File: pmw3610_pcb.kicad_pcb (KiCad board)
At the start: 2 copper layers, 23.5 x 31.5 mm, 24 parts, among them J1 Conn_01x06, J2 Conn_01x08, U1 PMW3610, U2 TLV74318PDBVR

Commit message: feat: update PCB rev 1.1
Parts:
- removed the TP1 at (145.2, 114.2)
- C1: footprint Capacitor_SMD:C_0603_1608Metric -> Capacitor_SMD:C_0805_2012Metric
- C4: value 100nF X7R -> 100nF
- C6: value 10uF X7R -> 10uF; footprint Capacitor_SMD:C_0603_1608Metric -> Capacitor_SMD:C_0805_2012Metric
- C7: value 10nF X7R -> 10nF
- H1, H2, H3, H4: moved to B.Cu
- J1: value Conn_01x06 -> Conn_PinHeader; footprint Connector_PinHeader_2.54mm:PinHeader_1x06_P2.54mm_Vertical -> Connector_PinHeader_2.54mm:PinHeader_1x07_P2.54mm_Vertical
- J2: value Conn_01x08 -> Conn_FPC
- moved J1 0.90 mm to (139.9, 92.8)
- moved C6 0.28 mm to (159.5, 107.8)
- moved C1 0.21 mm to (159.5, 100.2)
- turned H1 to 180 degrees
- turned H2 to 180 degrees
- turned H3 to 180 degrees
- turned H4 to 180 degrees
- renumbered TP4 to TP1
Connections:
- net VIO renamed VDDIO
- J2 pad 8: unconnected-(J2-Pin_8-Pad8) -> nRESET
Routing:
- net GND: track 15.9 -> 73.9 mm, vias 19 -> 42
- net nRESET: track 9.82 -> 32.7 mm, vias 2 -> 0
- net MOTION: track 30.7 -> 32.8 mm
- net VIN: track 30.9 -> 28.8 mm
- net +1V8: track 29.2 -> 31.1 mm
- net nCS: track 30.9 -> 32.5 mm
- net VDDIO: track 43.3 -> 42.2 mm
- net SCLK: track 20.5 -> 19.8 mm
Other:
- board text added: "${COMPANY} ${TITLE} Rev ${REVISION}"
- board text added: "JP1: [1-2 3]V_{DDIO}=VIN [1 2-3]V_{DDIO}=1.8V"
- board text added: "~{CS}"
- board text added: "~{RST}"
- board text removed: "${TITLE} Rev ${REVISION}"
- board text removed: "JP1: [1-2 3]VIO=VIN [1 2-3]VIO=1.8V"
- board text removed: "nCS"

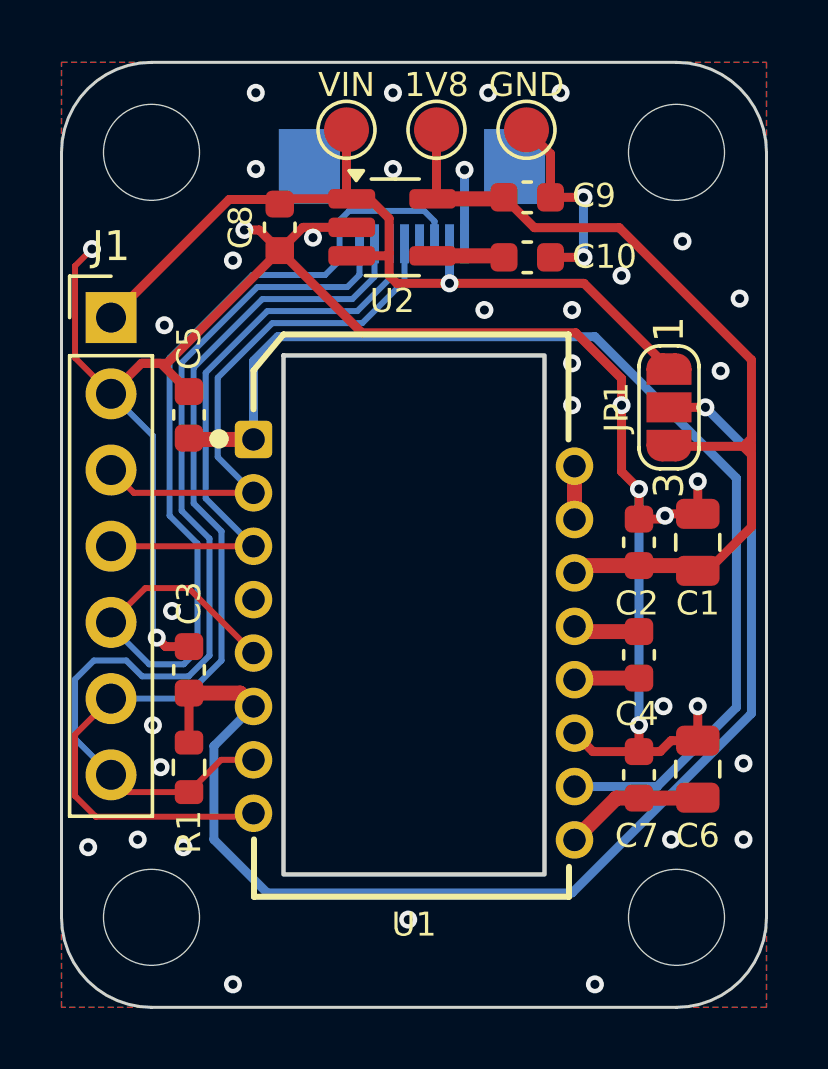
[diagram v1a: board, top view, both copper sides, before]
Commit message: feat: update PMW3610 footprint
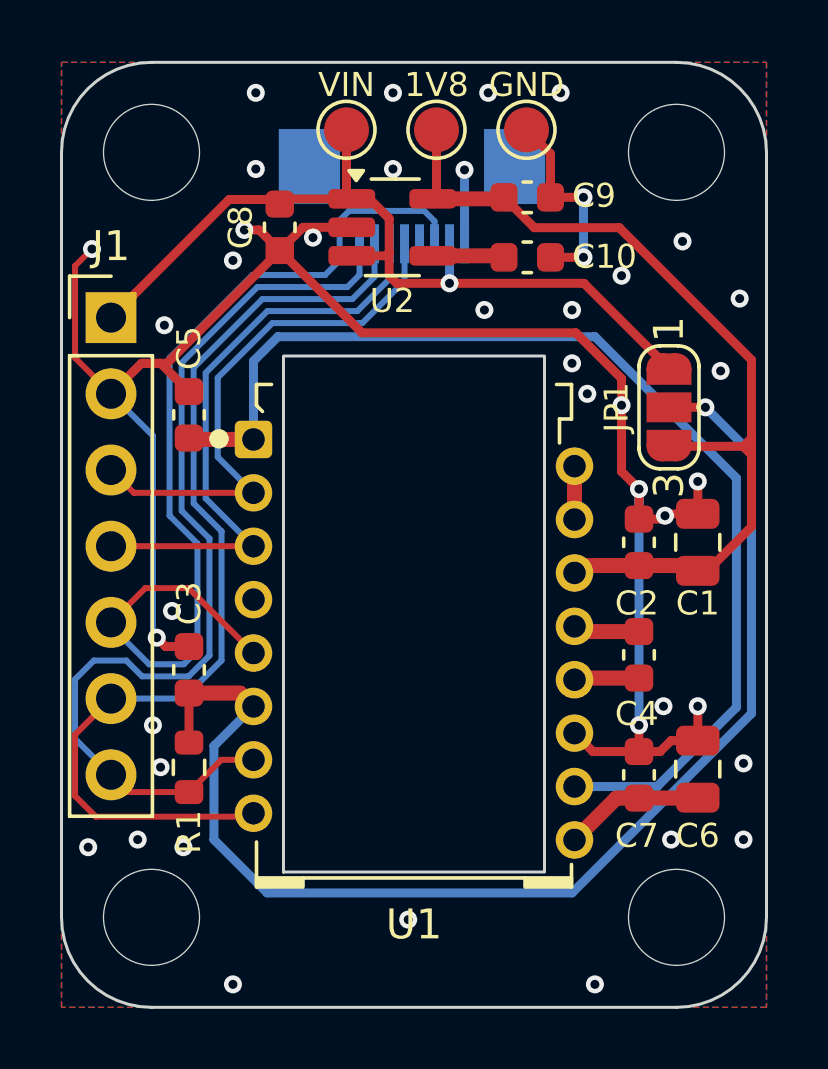
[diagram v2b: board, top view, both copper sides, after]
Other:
- board text added: "MOT"
- board text removed: "Mot"

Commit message: feat: increase the copper to board edge clearance to 0.4mm for better V-cut panelization
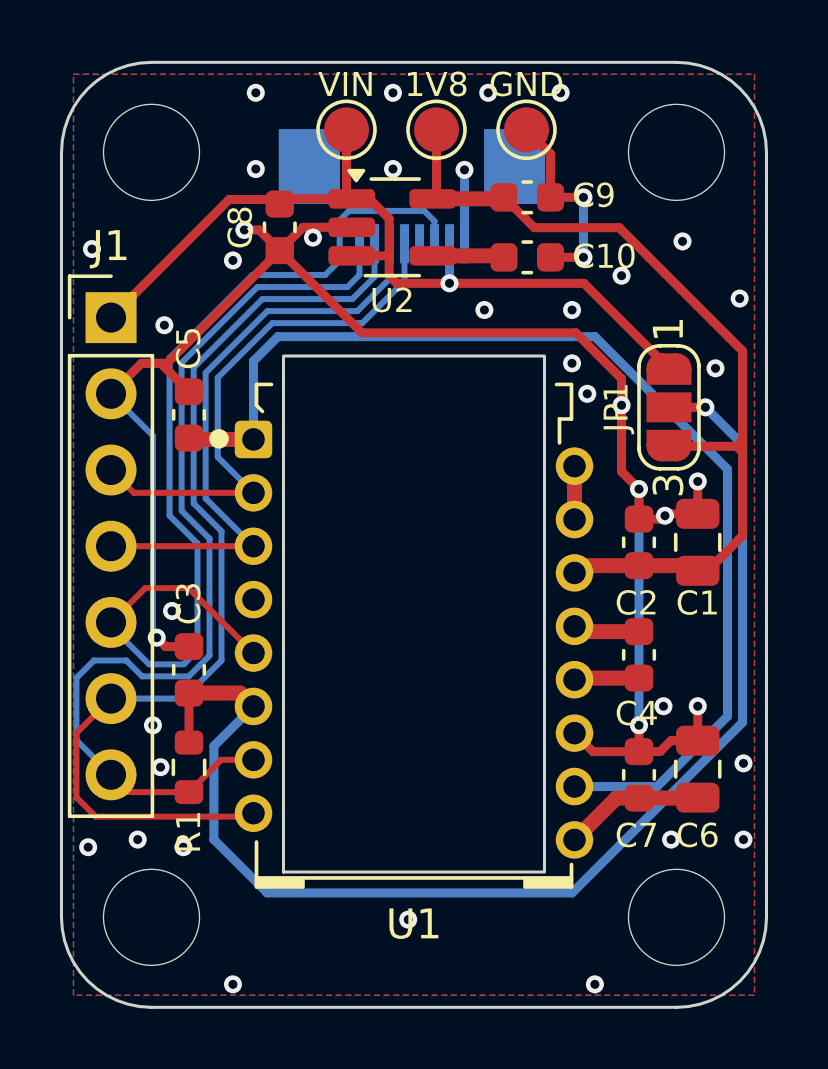
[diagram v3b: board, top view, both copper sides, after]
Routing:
- net GND: track 73.9 -> 68.3 mm
- net +1V8: track 31.1 -> 30.4 mm

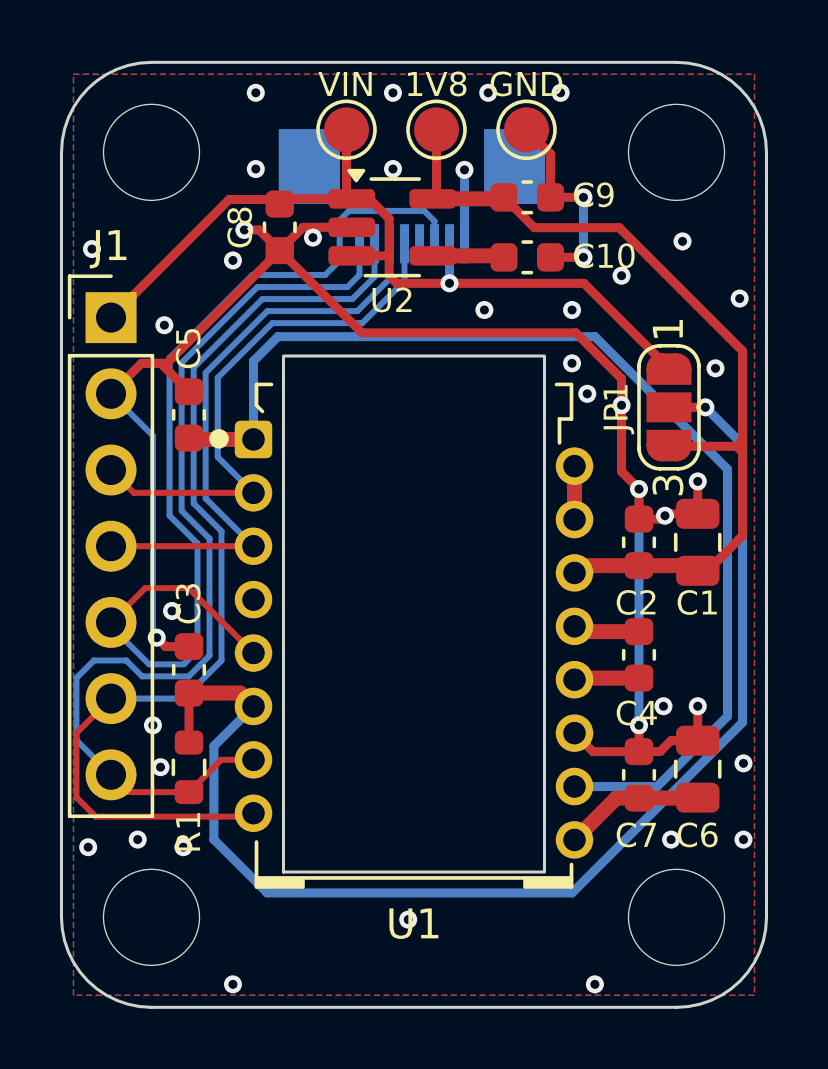
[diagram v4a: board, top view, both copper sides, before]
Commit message: feat: changed the J2 to the top layer
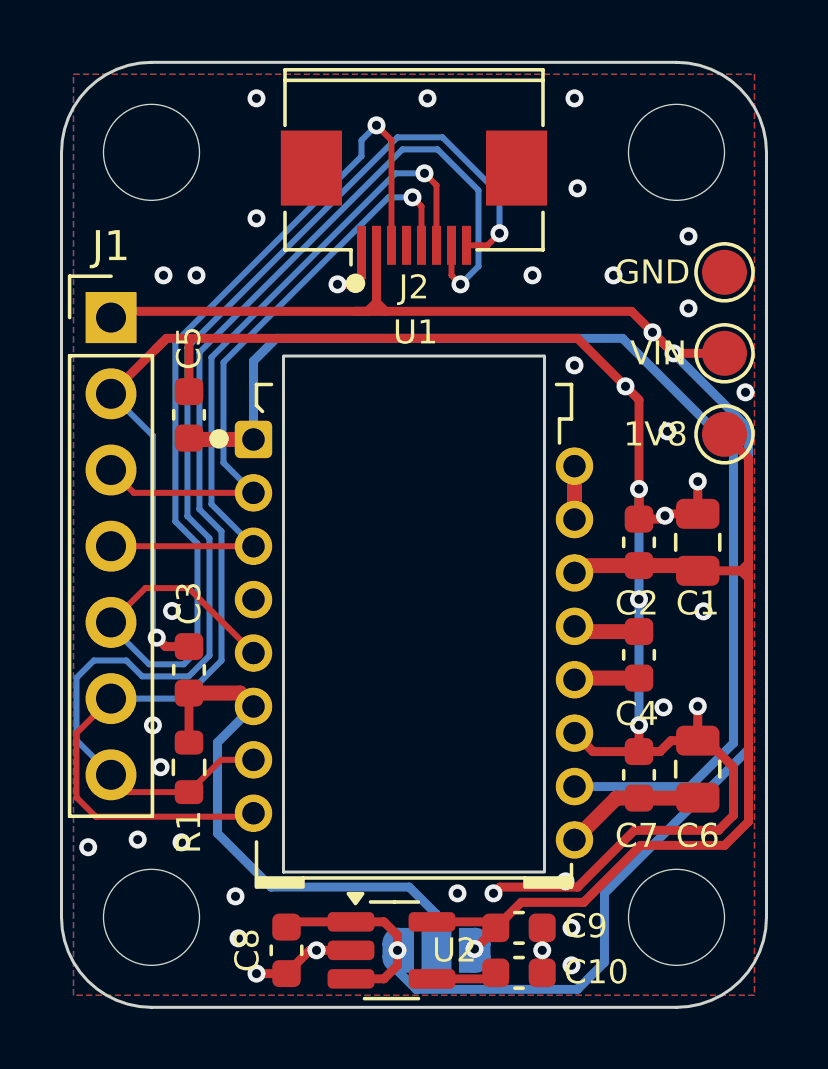
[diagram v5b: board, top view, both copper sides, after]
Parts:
- J2: moved to F.Cu
- JP1: moved to B.Cu
- moved C9 24.4 mm to (153.5, 113.1)
- moved C8 24.1 mm to (145.8, 113.8)
- moved U2 24.1 mm to (149.2, 113.8)
- moved C10 23.9 mm to (153.5, 114.6)
- moved JP1 19.7 mm to (150.8, 113.8), turned to 0 degrees
- moved TP2 14.6 mm to (160.3, 94.0)
- moved TP3 14.0 mm to (160.3, 96.7)
- moved TP1 8.13 mm to (160.3, 91.2)
- moved J2 0.08 mm to (150.0, 87.3), turned to 0 degrees
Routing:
- net VIN: track 28.8 -> 63.5 mm, vias 1 -> 3
- net VDDIO: track 41.9 -> 18.3 mm, vias 1 -> 0
- net MOTION: track 32.7 -> 42.3 mm, vias 0 -> 1
- net nRESET: track 32.6 -> 41.6 mm, vias 0 -> 1
- net SCLK: track 19.8 -> 23.8 mm, vias 0 -> 1
- net +1V8: track 30.4 -> 33.4 mm, vias 0 -> 1
- net nCS: track 32.5 -> 34.6 mm, vias 0 -> 1
- net GND: track 68.3 -> 70.3 mm, vias 42 -> 41
- net SDIO: track 18.2 -> 20.1 mm, vias 0 -> 1
- net Net-(U1-+VCSEL): track 37.1 -> 38.3 mm
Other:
- board text added: "JLCJLCJLCJLC"

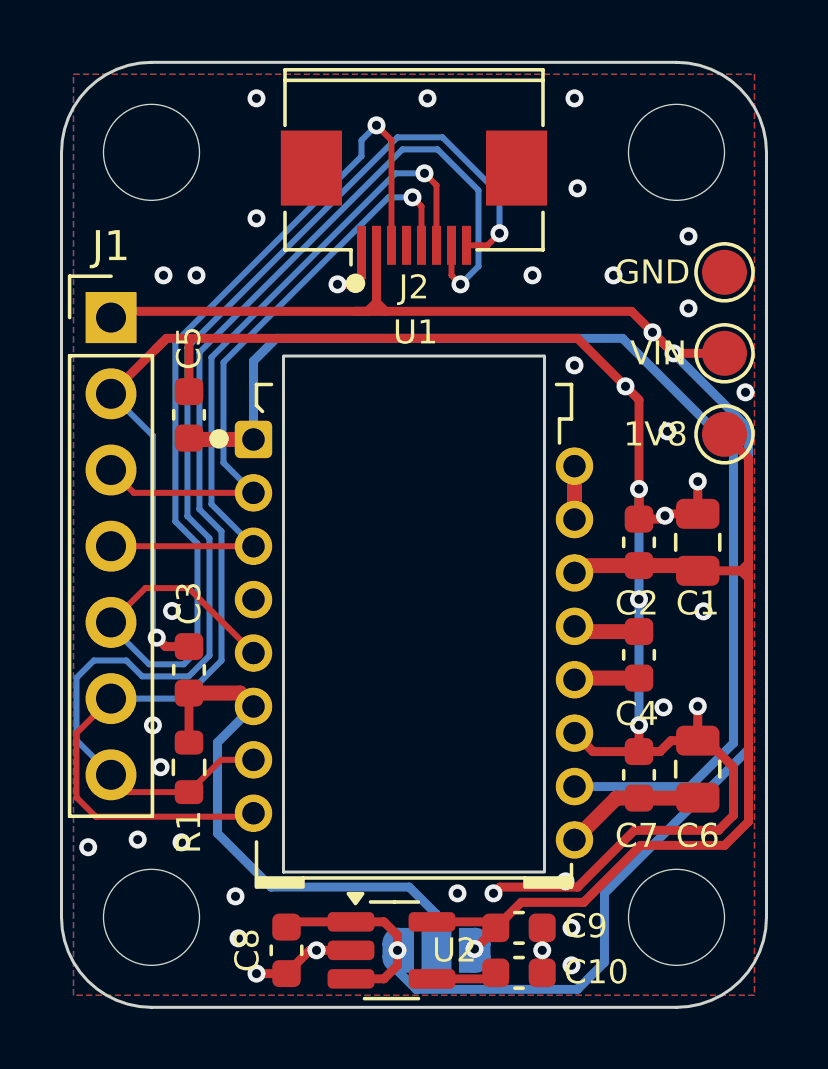
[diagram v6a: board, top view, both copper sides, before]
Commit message: feat: add axis mark
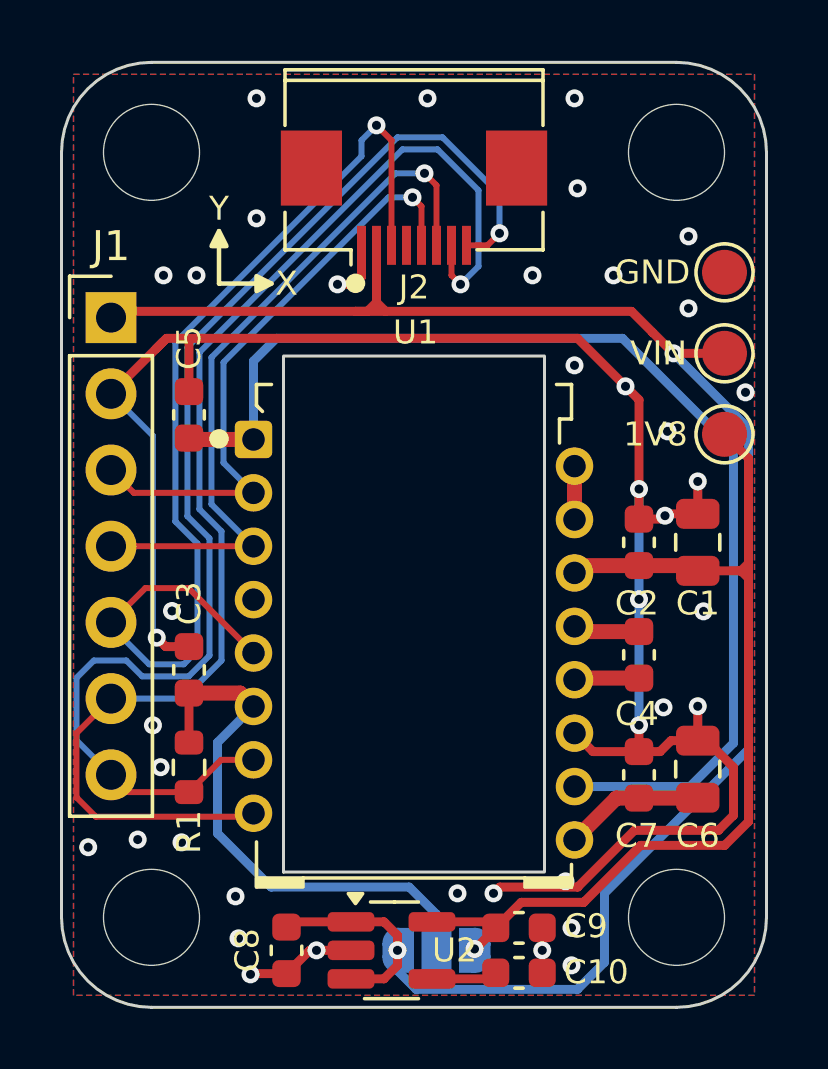
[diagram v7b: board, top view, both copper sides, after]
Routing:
- net VIN: track 63.5 -> 62.5 mm, vias 3 -> 2
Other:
- board text added: "X"
- board text added: "Y"
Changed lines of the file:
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@@
+		(layer "F.SilkS")
+	)
+	(gr_poly
+		(pts
+			(xy 144.75 91.375) (xy 145.25 91.625) (xy 144.75 91.875)
+		)
+		(stroke
+			(width 0.15)
+			(type solid)
+		)
+		(fill yes)
+		(layer "F.SilkS")
+	)
+	(gr_line
+		(start 143.5 89.875)
+		(end 143.5 91.625)
+		(stroke
+			(width 0.15)
+			(type default)
+		)
+		(layer "F.SilkS")
+	)
+	(gr_poly
+		(pts
+			(xy 143.25 90.375) (xy 143.5 89.875) (xy 143.75 90.375)
+		)
+		(stroke
+			(width 0.15)
+			(type solid)
+		)
+		(fill yes)
+		(layer "F.SilkS")
+	)
+	(gr_line
+		(start 143.5 91.625)
+		(end 145.25 91.625)
+		(stroke
+			(width 0.15)
+			(type default)
+		)
 		(layer "F.SilkS")
 	)
@@
 		(layer "Edge.Cuts")
 	)
+	(gr_text "Y"
+		(at 143.5 89.125 0)
+		(layer "F.SilkS")
+		(effects
+			(font
+				(size 0.8 0.8)
+				(thickness 0.125)
+			)
+		)
+	)
+	(gr_text "X"
+		(at 145.75 91.625 0)
+		(layer "F.SilkS")
+		(effects
+			(font
+				(size 0.8 0.8)
+				(thickness 0.125)
+			)
+		)
+	)
 	(gr_text "~{CS}"
 		(at 140.917 103.046 0)
@@
 	)
 	(segment
+		(start 144.55 114.65)
+		(end 144.575 114.625)
+		(width 0.3)
+		(layer "F.Cu")
+		(net 1)
+	)
+	(segment
 		(start 141.75 93.45)
 		(end 141.4 93.8)
@@
 	)
 	(segment
+		(start 144.575 114.625)
+		(end 145.75 114.625)
+		(width 0.3)
+		(layer "F.Cu")
+		(net 1)
+	)
+	(segment
 		(start 157.5 98.474)
 		(end 157.5 99.475)
@@
 	)
 	(segment
-		(start 144.75 114.625)
-		(end 145.75 114.625)
-		(width 0.3)
-		(layer "F.Cu")
-		(net 1)
-	)
-	(segment
 		(start 160.65 109.35)
 		(end 160.65 107.75)
@@
 	)
 	(via
-		(at 144.75 114.625)
+		(at 144.55 114.65)
 		(size 0.6)
 		(drill 0.3)
@@
 	)
 	(via
-		(at 157.95 93.25)
-		(size 0.6)
-		(drill 0.3)
-		(layers "F.Cu" "B.Cu")
-		(net 4)
-	)
-	(via
 		(at 158.65 93.95)
 		(size 0.6)
@@
 		(start 161.15 96.45)
 		(end 161.15 107.15)
-		(width 0.3)
-		(layer "B.Cu")
-		(net 4)
-	)
-	(segment
-		(start 158.65 93.95)
-		(end 157.95 93.25)
 		(width 0.3)
 		(layer "B.Cu")
@@
 		)
 	)
+	(group ""
+		(members "59092b9a-5ab1-4de8-a233-80c866215d1d" "984f2c04-1341-4ce4-8f0e-4d99df58a4ad"
+			"9c69163a-cfd1-4b06-9f9e-7636db41e523" "a245d391-8121-4a08-8cd4-61b815316893"
+			"a3ab3492-afca-4e26-8b79-5e16690a3640" "d44de8ec-e799-4010-b1aa-de5dd36afba8"
+		)
+	)

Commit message: feat: add jumper JP2 for FFC/FPC and nRESET pin
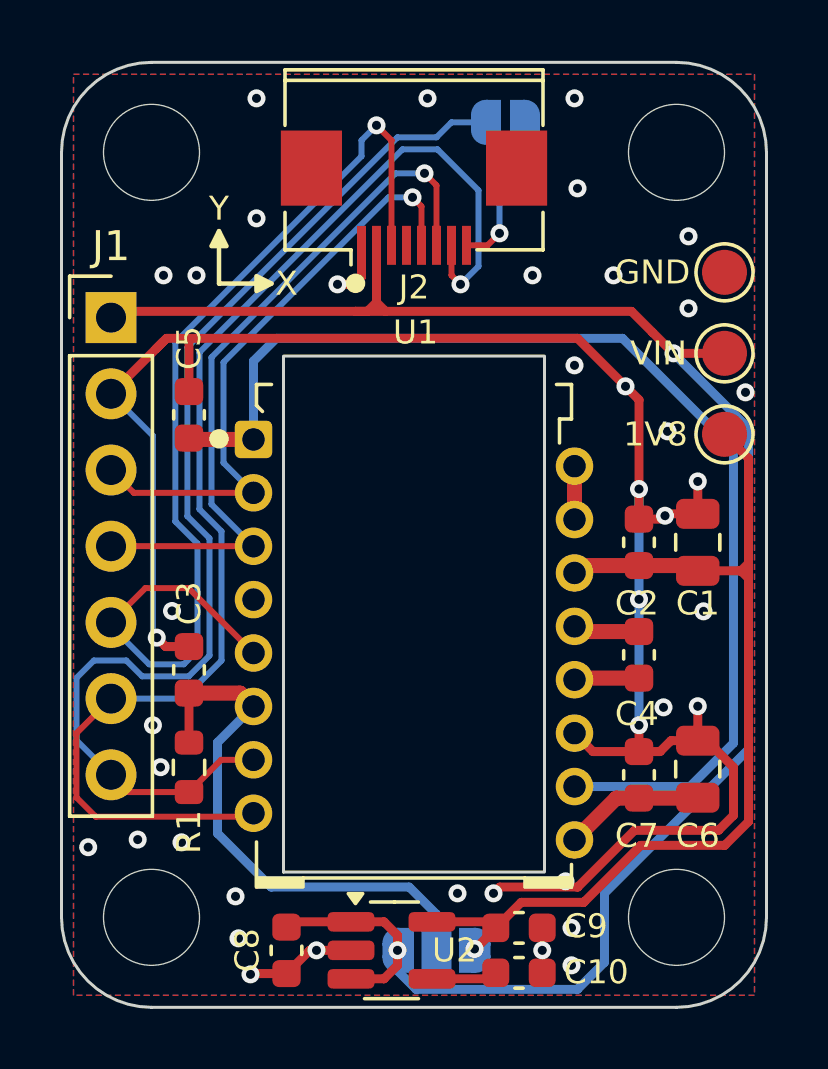
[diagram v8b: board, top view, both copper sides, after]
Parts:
- added JP2: FPC_RST, Jumper:SolderJumper-2_P1.3mm_Open_RoundedPad1.0x1.5mm, B.Cu at (153.1, 86.2)
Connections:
- J2 pad 8: nRESET -> Net-(J2-Pin_8)
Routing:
- net Net-(J2-Pin_8): track 0.00 -> 5.32 mm, vias 0 -> 1
- net nRESET: track 41.6 -> 38.0 mm, vias 1 -> 0
